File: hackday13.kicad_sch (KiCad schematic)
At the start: 18 parts, among them J1 TT-output, J2 TT-input, J3 TT-bidirectional, SW1 Reset button, SW2 SW_DIP_x02, U1 RaspberryPi_Pico

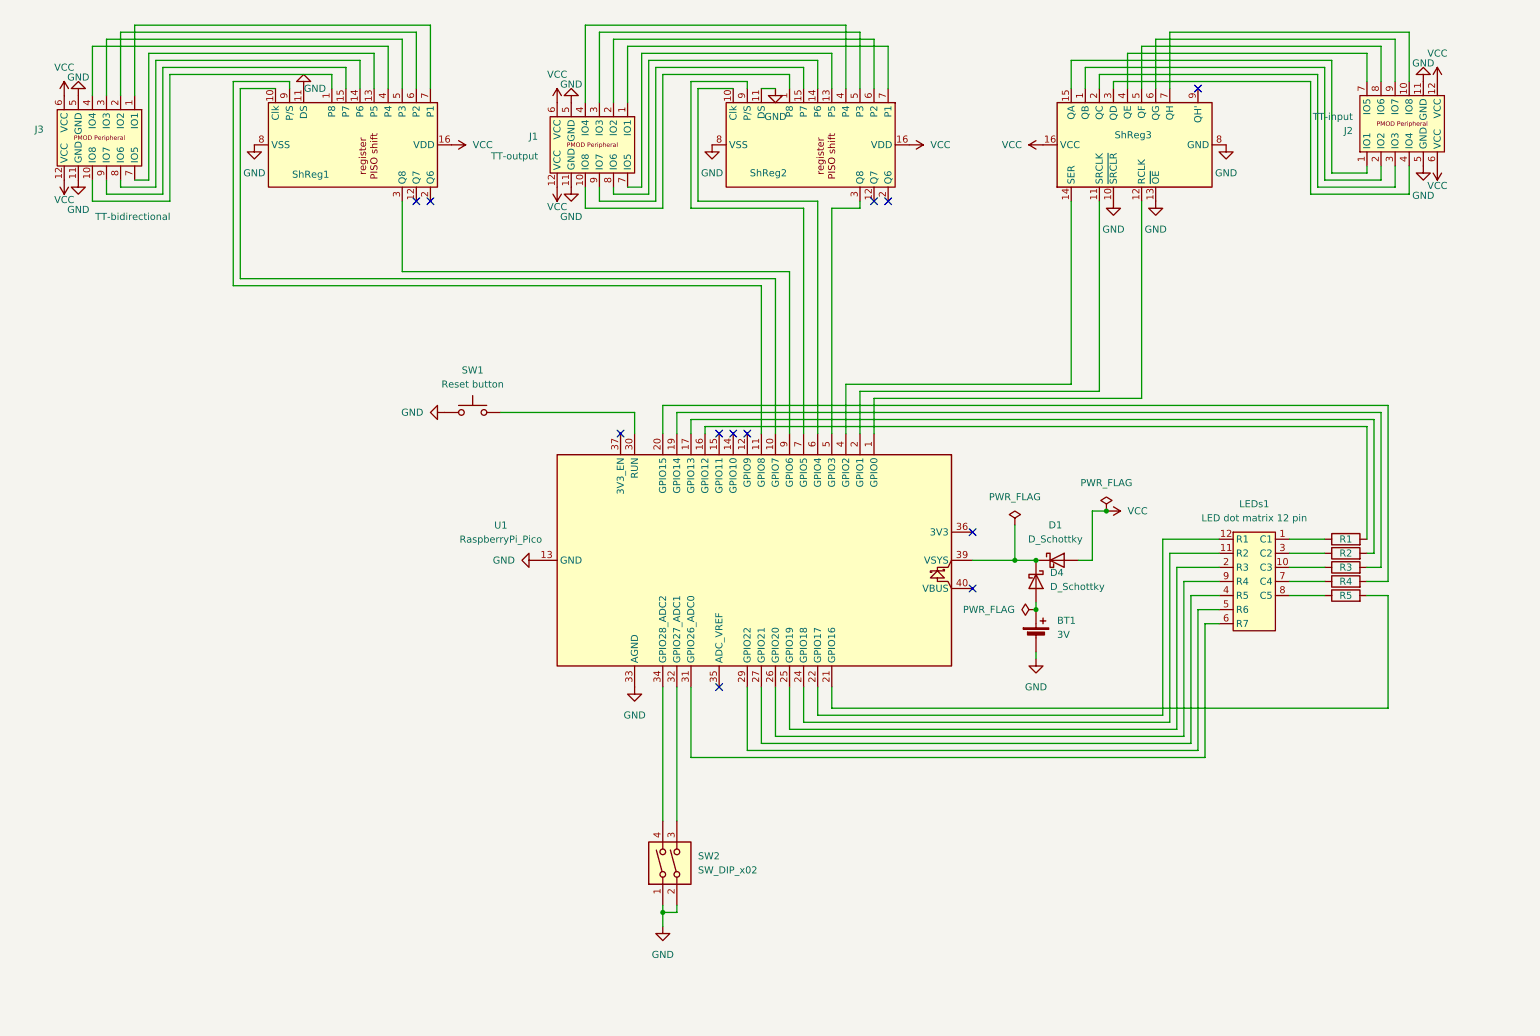
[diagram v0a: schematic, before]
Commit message: [proj/schematic] Update Project to KiCad Vers. 9.0.X + add Li-Ion Charger to schematic
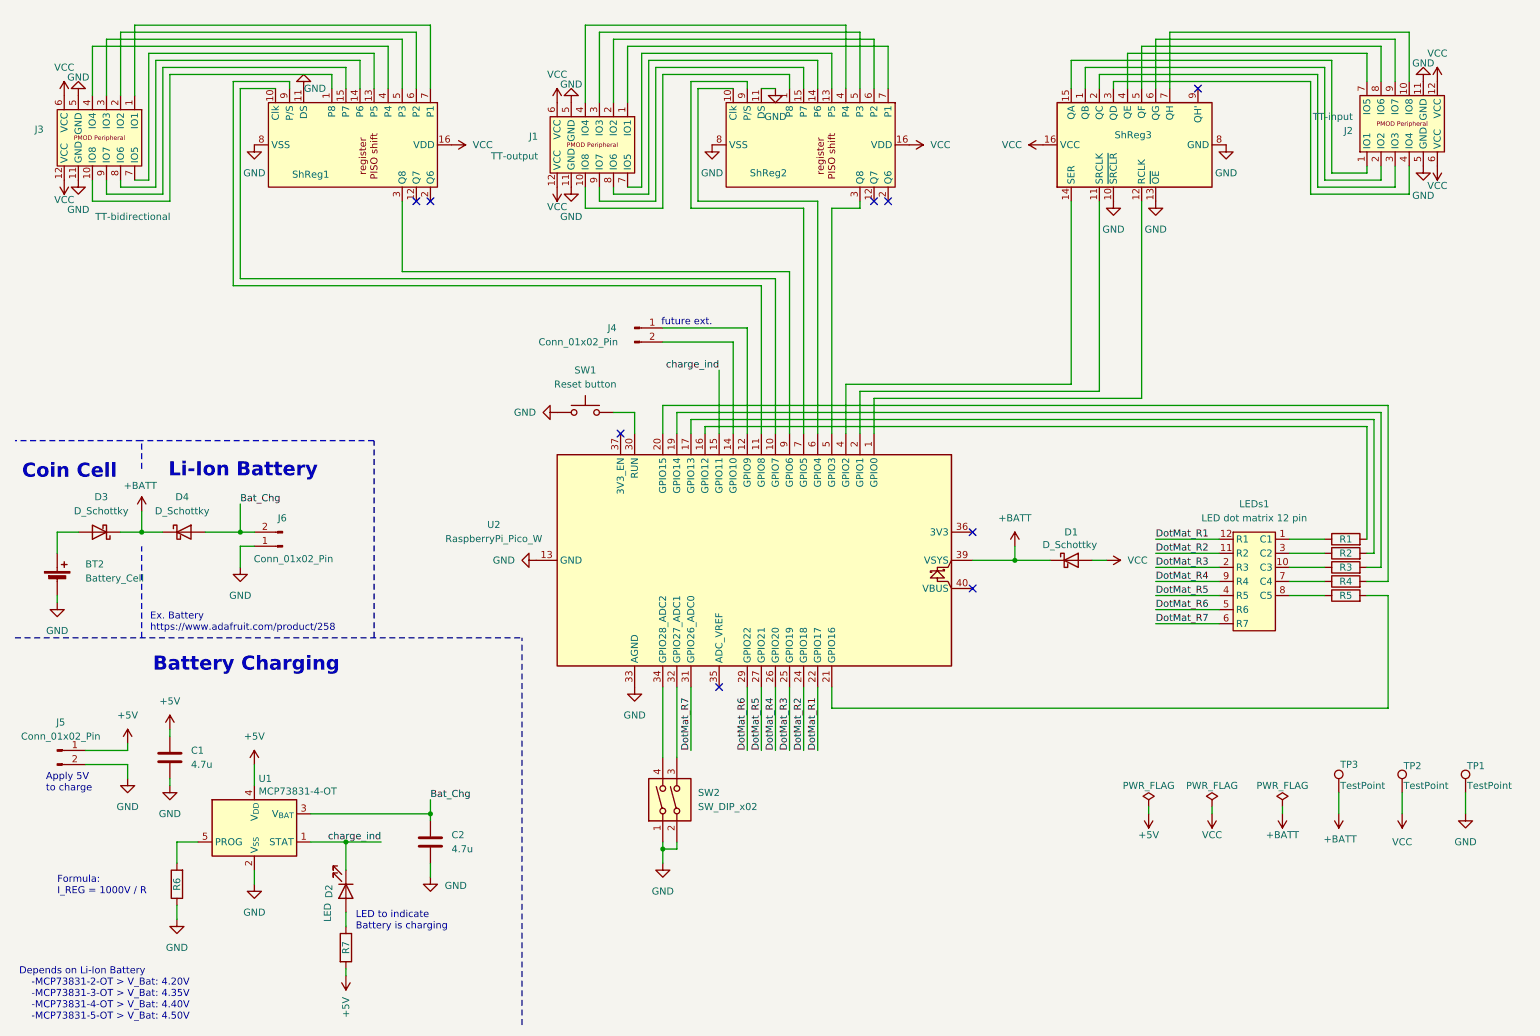
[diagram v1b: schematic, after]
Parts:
- removed BT1: 3V, Battery:BatteryHolder_Keystone_3002_1x2032, symbol Device:Battery_Cell
- removed U1: RaspberryPi_Pico, Module_RaspberryPi_Pico:RaspberryPi_Pico_Common, symbol MCU_Module_RaspberryPi_Pico:RaspberryPi_Pico
- added BT2: Battery_Cell, Battery:BatteryHolder_Keystone_3002_1x2032, symbol Device:Battery_Cell
- added C1, C2: 4.7u, symbol Device:C
- added D2: LED, symbol Device:LED
- added D3: D_Schottky, Diode_THT:D_DO-35_SOD27_P7.62mm_Horizontal, symbol Device:D_Schottky
- added J4, J5: Conn_01x02_Pin, Connector_PinHeader_2.54mm:PinHeader_1x02_P2.54mm_Vertical, symbol Connector:Conn_01x02_Pin
- added J6: Conn_01x02_Pin, Connector_JST:JST_PH_B2B-PH-K_1x02_P2.00mm_Vertical, symbol Connector:Conn_01x02_Pin
- added R6: 2k, Resistor_THT:R_Axial_DIN0207_L6.3mm_D2.5mm_P10.16mm_Horizontal, symbol Device:R
- added R7: 1000 Ohm, Resistor_THT:R_Axial_DIN0207_L6.3mm_D2.5mm_P10.16mm_Horizontal, symbol Device:R
- added TP1, TP2, TP3: TestPoint, TestPoint:TestPoint_Pad_D3.0mm, symbol Connector:TestPoint
- added U1: MCP73831-4-OT, Package_TO_SOT_SMD:SOT-23-5, symbol Battery_Management:MCP73831-4-OT
- added U2: RaspberryPi_Pico_W, Module_RaspberryPi_Pico:RaspberryPi_Pico_Common, symbol MCU_Module_RaspberryPi_Pico:RaspberryPi_Pico_W
- LEDs1: value LED dot matrix 12 pin -> LED dot matrix 12 pin
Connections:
- net GND: now also BT2.2 (-), C1.2, C2.2, J5.2 (Pin_2), J6.1 (Pin_1), R6.1, TP1.1, U1.2 (V_{SS}), U2.13 (GND), U2.18 (GND), U2.23 (GND), U2.28 (GND), U2.3 (GND), U2.33 (AGND), U2.38 (GND), U2.8 (GND)
- net VCC: now also TP2.1
- net at ShReg1.10 (Clk): now also U2.10 (GPIO7)
- net at ShReg1.3 (Q8): now also U2.9 (GPIO6)
- net at ShReg1.9 (P/S): now also U2.11 (GPIO8)
- net at R2.2: now also U2.17 (GPIO13)
- net at SW1.2: now also U2.30 (RUN)
- net at R3.2: now also U2.19 (GPIO14)
- net at R1.2: now also U2.16 (GPIO12)
- net +BATT: now reaches D1.1 (K), D4.1 (K)
- net +BATT: now also D3.1 (K), TP3.1, U2.39 (VSYS)
- net Bat_Chg: now reaches D4.2 (A)
- net Bat_Chg: now also C2.1, J6.2 (Pin_2), U1.3 (V_{BAT})
- net at SW2.3: now also U2.32 (GPIO27_ADC1)
- net at SW2.4: now also U2.34 (GPIO28_ADC2)
- net at R4.2: now also U2.20 (GPIO15)
- net at ShReg3.11 (SRCLK): now also U2.2 (GPIO1)
- net at ShReg3.12 (RCLK): now also U2.1 (GPIO0)
- net at ShReg3.14 (SER): now also U2.4 (GPIO2)
- net at R5.2: now also U2.21 (GPIO16)
- net at ShReg2.10 (Clk): now also U2.6 (GPIO4)
- net at ShReg2.3 (Q8): now also U2.5 (GPIO3)
- net at ShReg2.9 (P/S): now also U2.7 (GPIO5)
- net DotMat_R2: now reaches LEDs1.11 (R2)
- net DotMat_R2: now also U2.24 (GPIO18)
- net DotMat_R1: now reaches LEDs1.12 (R1)
- net DotMat_R1: now also U2.22 (GPIO17)
- net DotMat_R3: now reaches LEDs1.2 (R3)
- net DotMat_R3: now also U2.25 (GPIO19)
- net DotMat_R5: now reaches LEDs1.4 (R5)
- net DotMat_R5: now also U2.27 (GPIO21)
- net DotMat_R6: now reaches LEDs1.5 (R6)
- net DotMat_R6: now also U2.29 (GPIO22)
- net DotMat_R7: now reaches LEDs1.6 (R7)
- net DotMat_R7: now also U2.31 (GPIO26_ADC0)
- net DotMat_R4: now reaches LEDs1.9 (R4)
- net DotMat_R4: now also U2.26 (GPIO20)
- new net: BT2.1 (+), D3.2 (A)
- new net: J4.1 (Pin_1), U2.12 (GPIO9)
- new net: J4.2 (Pin_2), U2.14 (GPIO10)
- new net: R6.2, U1.5 (PROG)
- new net: D2.2 (A), R7.1
- new net +5V: C1.1, J5.1 (Pin_1), R7.2, U1.4 (V_{DD})
- new net charge_ind: D2.1 (K), U1.1 (STAT), U2.15 (GPIO11)
- no-connect marks 12 -> 9
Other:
- note added: "Apply 5V to charge"
- note added: "Battery Charging"
- note added: "Coin Cell"
- note added: "Depends on Li-Ion Battery -MCP73831-2-OT > V_Bat: 4.20V -MCP73831-3-OT > V_Bat: 4.35V -MCP73831-4-OT > V_Bat: 4.40V -MCP73831-5-OT > V_Bat: 4.50V"
- note added: "Ex. Battery https://www.adafruit.com/product/258"
- note added: "Formula: I_REG = 1000V / R"
- note added: "LED to indicate Battery is charging"
- note added: "Li-Ion Battery"
- note added: "future ext."
- moved on the sheet: D1, D4, SW1, SW2

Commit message: [layout] Start with new 4-L layout
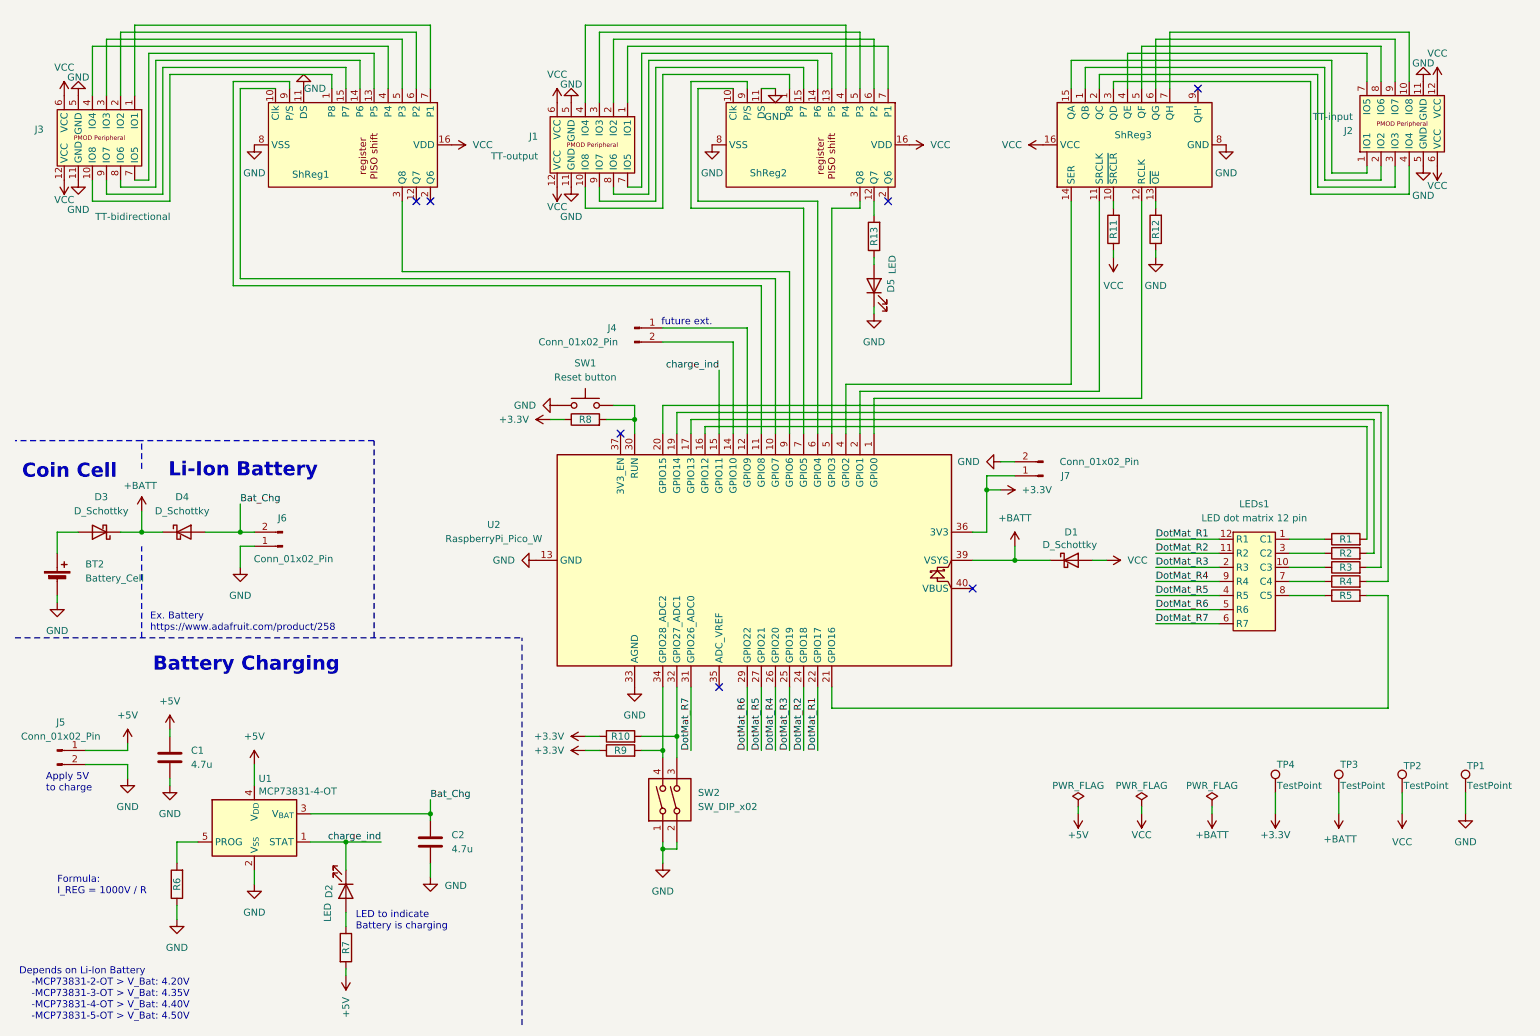
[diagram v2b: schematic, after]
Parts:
- added D5: LED, LED_THT:LED_D3.0mm, symbol Device:LED
- added J7: Conn_01x02_Pin, Connector_PinHeader_2.54mm:PinHeader_1x02_P2.54mm_Vertical, symbol Connector:Conn_01x02_Pin
- added R10, R8, R9: 1k, Resistor_THT:R_Axial_DIN0207_L6.3mm_D2.5mm_P10.16mm_Horizontal, symbol Device:R
- added R11, R12: 0, Resistor_THT:R_Axial_DIN0207_L6.3mm_D2.5mm_P10.16mm_Horizontal, symbol Device:R
- added R13: 1000 Ohm, Resistor_THT:R_Axial_DIN0207_L6.3mm_D2.5mm_P10.16mm_Horizontal, symbol Device:R
- added TP4: TestPoint, TestPoint:TestPoint_Pad_D3.0mm, symbol Connector:TestPoint
- C1, C2: footprint (none) -> Capacitor_THT:C_Disc_D7.0mm_W2.5mm_P5.00mm
- D2: footprint (none) -> LED_THT:LED_D3.0mm
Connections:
- net GND: now also D5.1 (K), J7.2 (Pin_2), R12.1; no longer ShReg3.10 (~{SRCLR}), ShReg3.13 (~{OE})
- net VCC: now also R11.1
- net at SW1.2, U2.30 (RUN): now also R8.2
- net at SW2.3, U2.32 (GPIO27_ADC1): now also R10.2
- net at SW2.4, U2.34 (GPIO28_ADC2): now also R9.2
- net +3.3V: now reaches U2.36 (3V3)
- net +3.3V: now also J7.1 (Pin_1), R10.1, R8.1, R9.1, TP4.1
- net at ShReg2.12 (Q7): now also R13.2
- new net: D5.2 (A), R13.1
- new net: R11.2, ShReg3.10 (~{SRCLR})
- new net: R12.2, ShReg3.13 (~{OE})
- no-connect marks 9 -> 7
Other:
- moved on the sheet: SW1

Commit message: [layout] first version of possible layout - review required
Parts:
- removed J4: Conn_01x02_Pin, Connector_PinHeader_2.54mm:PinHeader_1x02_P2.54mm_Vertical, symbol Connector:Conn_01x02_Pin
- removed ShReg1, ShReg2: MC14014B, Package_SO:SOIC-16_3.9x9.9mm_P1.27mm, symbol custom_components_led_pcb:MC14014B
- removed ShReg3: 74HC595, Package_SO:SOIC-16_3.9x9.9mm_P1.27mm, symbol 74xx:74HC595
- added C3, C4, C5: 100n, Capacitor_THT:C_Disc_D7.0mm_W2.5mm_P5.00mm, symbol Device:C
- added D6: LED, LED_THT:LED_D3.0mm, symbol Device:LED
- added H1, H2, H3, H4: MountingHole, MountingHole:MountingHole_3.2mm_M3, symbol Mechanical:MountingHole
- added J8: Conn_01x03_Pin, Connector_PinHeader_2.54mm:PinHeader_1x03_P2.54mm_Vertical, symbol Connector:Conn_01x03_Pin
- added R14, R15: 0, Resistor_SMD:R_0805_2012Metric, symbol Device:R
- added R16: 2.2k Ohm, Resistor_THT:R_Axial_DIN0207_L6.3mm_D2.5mm_P10.16mm_Horizontal, symbol Device:R
- added U3: 74HC595, Package_DIP:DIP-16_W7.62mm, symbol 74xx:74HC595
- added U4, U5: 74HC165, Package_DIP:DIP-16_W7.62mm, symbol 74xx:74HC165
- R11: footprint Resistor_THT:R_Axial_DIN0207_L6.3mm_D2.5mm_P10.16mm_Horizontal -> Resistor_SMD:R_0805_2012Metric
- R12: value 0 -> 2.2k Ohm
- R13: value 1000 Ohm -> 0; footprint Resistor_THT:R_Axial_DIN0207_L6.3mm_D2.5mm_P10.16mm_Horizontal -> Resistor_SMD:R_0805_2012Metric
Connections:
- net DotMat_R1: now also U2.24 (GPIO18); no longer U2.22 (GPIO17)
- net DotMat_R2: now also U2.25 (GPIO19); no longer U2.24 (GPIO18)
- net DotMat_R3: now also U2.29 (GPIO22); no longer U2.25 (GPIO19)
- net DotMat_R4: now also U2.27 (GPIO21); no longer U2.26 (GPIO20)
- net DotMat_R5: now also U2.31 (GPIO26_ADC0); no longer U2.27 (GPIO21)
- net DotMat_R6: now also U2.32 (GPIO27_ADC1); no longer U2.29 (GPIO22)
- net DotMat_R7: now also U2.34 (GPIO28_ADC2); no longer U2.31 (GPIO26_ADC0)
- net GND: now also R13.1, C3.2, C4.2, C5.2, R14.2, R15.2, U3.8 (GND), U4.8 (GND), U5.8 (GND); no longer D5.1 (K), R12.1
- net VCC: now also R12.2, C3.1, C4.1, C5.1, R16.2, U3.16 (VCC), U4.16 (VCC), U5.16 (VCC)
- net INOUT_8: now reaches J3.10 (IO8)
- net INOUT_8: now also U4.11 (D0)
- net OPS: now reaches U2.10 (GPIO7)
- net OPS: now also U4.1 (~{PL}), U5.1 (~{PL})
- net INOUT_5: now reaches J3.7 (IO5)
- net INOUT_5: now also U4.5 (D6)
- net INOUT_6: now reaches J3.8 (IO6)
- net INOUT_6: now also U4.3 (D4)
- net INOUT_7: now reaches J3.9 (IO7)
- net INOUT_7: now also U4.13 (D2)
- net CLK: now reaches U2.9 (GPIO6)
- net CLK: now also U4.2 (CP), U5.2 (CP)
- net INOUT_4: now reaches J3.4 (IO4)
- net INOUT_4: now also U4.12 (D1)
- net INOUT_3: now reaches J3.3 (IO3)
- net INOUT_3: now also U4.14 (D3)
- net INOUT_2: now reaches J3.2 (IO2)
- net INOUT_2: now also U4.4 (D5)
- net INOUT_1: now reaches J3.1 (IO1)
- net INOUT_1: now also U4.6 (D7)
- net at U2.11 (GPIO8): now also J8.1 (Pin_1)
- net at R9.2, SW2.4: now also U2.22 (GPIO17); no longer U2.34 (GPIO28_ADC2)
- net DotMat_C4: now reaches U2.17 (GPIO13)
- net DotMat_C4: now also R4.2; no longer R2.2
- net DotMat_C2: now reaches R3.2
- net DotMat_C2: now also U2.20 (GPIO15); no longer U2.19 (GPIO14)
- net DotMat_C1: now reaches R1.2
- net DotMat_C1: now also U2.26 (GPIO20); no longer U2.16 (GPIO12)
- net at D5.2 (A): now also R12.1; no longer R13.1
- net at R10.2, SW2.3: now also U2.21 (GPIO16); no longer U2.32 (GPIO27_ADC1)
- net IN2: now reaches J2.2 (IO2)
- net IN2: now also U3.2 (QC)
- net at R11.2: now also U3.10 (~{SRCLR})
- net at U2.2 (GPIO1): now also U3.11 (SRCLK)
- net at U2.1 (GPIO0): now also U3.12 (RCLK)
- net at U2.4 (GPIO2): now also U3.14 (SER)
- net IN1: now reaches J2.1 (IO1)
- net IN1: now also U3.3 (QD)
- net IN3: now reaches J2.3 (IO3)
- net IN3: now also U3.4 (QE)
- net IN4: now reaches J2.4 (IO4)
- net IN4: now also U3.6 (QG)
- net IN5: now reaches J2.7 (IO5)
- net IN5: now also U3.15 (QA)
- net IN6: now reaches J2.8 (IO6)
- net IN6: now also U3.1 (QB)
- net IN7: now reaches J2.9 (IO7)
- net IN7: now also U3.5 (QF)
- net IN8: now reaches J2.10 (IO8)
- net IN8: now also U3.7 (QH)
- net at U2.12 (GPIO9): now also J8.2 (Pin_2)
- net at U2.14 (GPIO10): now also J8.3 (Pin_3)
- net DotMat_C3: now reaches R5.2
- net DotMat_C3: now also U2.19 (GPIO14); no longer U2.21 (GPIO16)
- net Set_Data_1: now reaches U2.5 (GPIO3)
- net Set_Data_1: now also U4.9 (Q7)
- net Set_Data_2: now reaches U2.6 (GPIO4)
- net Set_Data_2: now also U5.9 (Q7)
- net CLK_EN: now reaches U2.7 (GPIO5)
- net CLK_EN: now also U4.15 (~{CE}), U5.15 (~{CE})
- net OUT_1: now reaches J1.1 (IO1)
- net OUT_1: now also U5.6 (D7)
- net OUT_8: now reaches J1.10 (IO8)
- net OUT_8: now also U5.11 (D0)
- net OUT_2: now reaches J1.2 (IO2)
- net OUT_2: now also U5.4 (D5)
- net OUT_3: now reaches J1.3 (IO3)
- net OUT_3: now also U5.14 (D3)
- net OUT_4: now reaches J1.4 (IO4)
- net OUT_4: now also U5.12 (D1)
- net OUT_5: now reaches J1.7 (IO5)
- net OUT_5: now also U5.5 (D6)
- net OUT_6: now reaches J1.8 (IO6)
- net OUT_6: now also U5.3 (D4)
- net OUT_7: now reaches J1.9 (IO7)
- net OUT_7: now also U5.13 (D2)
- net at R13.2: now also U3.13 (~{OE})
- new net: D6.1 (K), U5.7 (~{Q7})
- new net: D6.2 (A), R16.1
- new net: D5.1 (K), U4.7 (~{Q7})
- new net: R14.1, U4.10 (DS)
- new net: R15.1, U5.10 (DS)
- new net DotMat_C5: R2.2, U2.16 (GPIO12)
- no-connect marks 7 -> 4
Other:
- moved on the sheet: R10, R9, SW2
